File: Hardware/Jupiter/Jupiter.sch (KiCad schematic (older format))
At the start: 93 parts

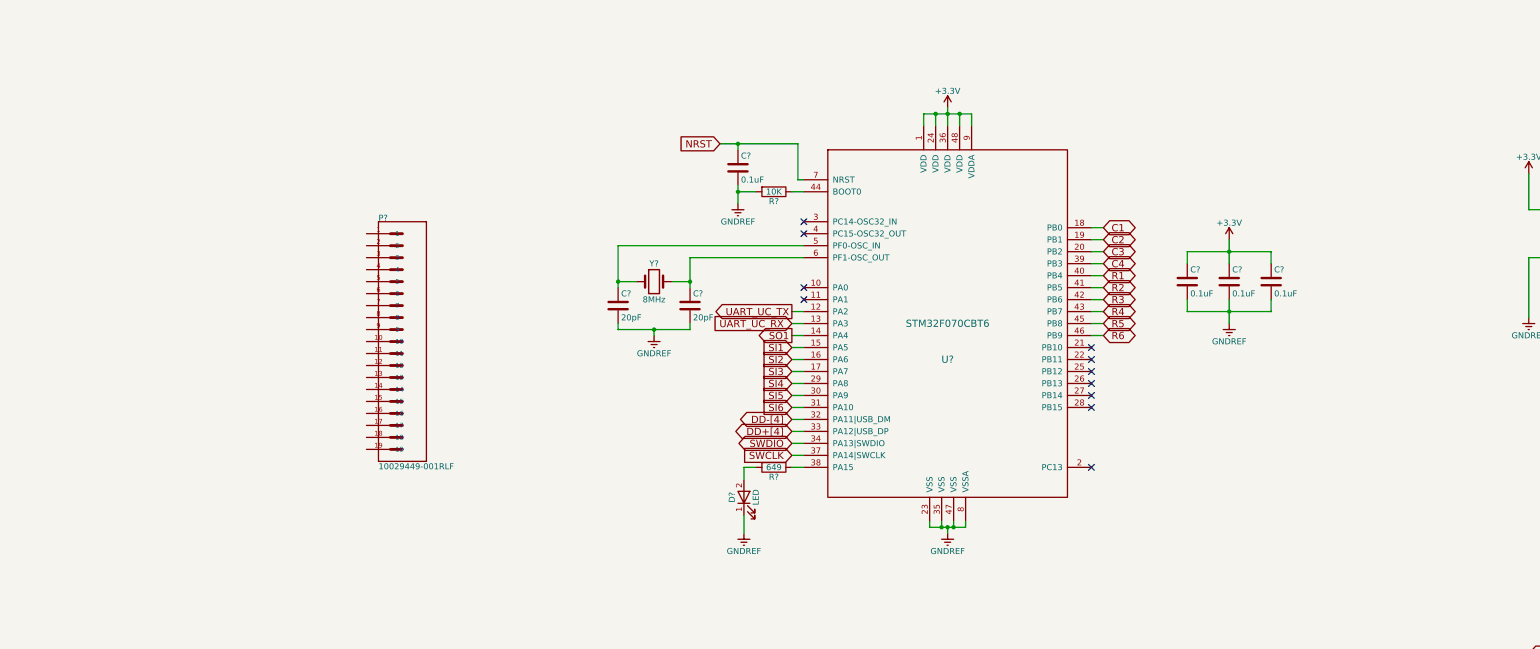
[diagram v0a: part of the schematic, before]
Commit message: Begin work for connecting HDMI transmitter interface IC to external HDMI connector.
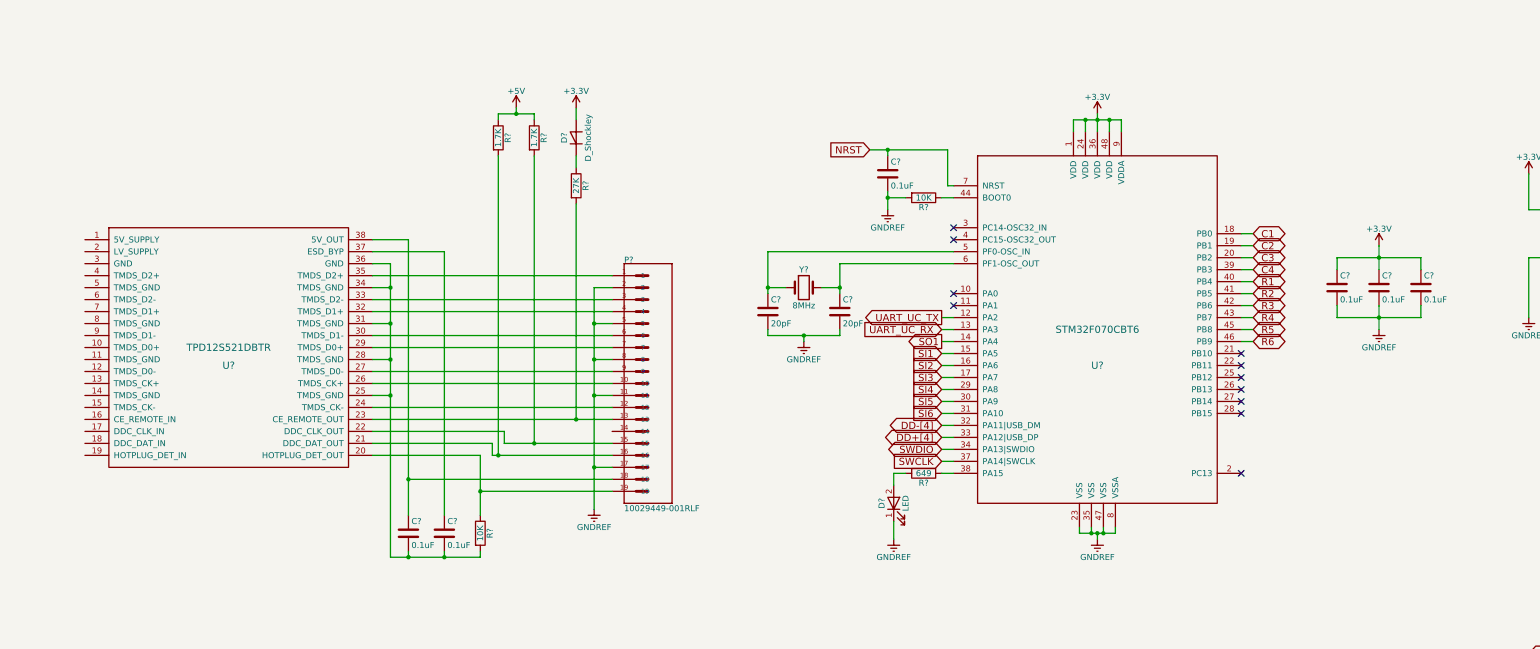
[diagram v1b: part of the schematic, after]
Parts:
- added C? (x2): 0.1uF, symbol C
- added D?: D_Shockley, symbol D_Shockley
- added R? (x2): 1.7K, symbol R
- added R?: 27K, symbol R
- added R?: 10K, symbol R
- added U?: TPD12S521DBTR, symbol TPD12S521DBTR
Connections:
- net +3V3: now also D?.2 (A)
- net +5V: now also R?.1, R?.1
- net GNDREF: now also P?.11, P?.17, P?.2, P?.5, P?.8
- net at P?.1: now also U?.35 (TMDS_D2+)
- net at P?.10: now also U?.26 (TMDS_CK+)
- net at P?.12: now also U?.24 (TMDS_CK-)
- net at P?.13: now also R?.2, U?.23 (CE_REMOTE_OUT)
- net at P?.15: now also R?.2, U?.22 (DDC_CLK_OUT)
- net at P?.16: now also R?.2, U?.21 (DDC_DAT_OUT)
- net at P?.18: now also C?.1, U?.38 (5V_OUT)
- net at P?.19: now also R?.1, U?.20 (HOTPLUG_DET_OUT)
- net at P?.3: now also U?.33 (TMDS_D2-)
- net at P?.4: now also U?.32 (TMDS_D1+)
- net at P?.6: now also U?.30 (TMDS_D1-)
- net at P?.7: now also U?.29 (TMDS_D0+)
- net at P?.9: now also U?.27 (TMDS_D0-)
- new net: C?.2, C?.2, R?.2, U?.25 (TMDS_GND), U?.28 (TMDS_GND), U?.31 (TMDS_GND), U?.34 (TMDS_GND), U?.36 (GND)
- new net: C?.1, U?.37 (ESD_BYP)
- new net: D?.1 (K), R?.1
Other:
- moved on the sheet: C?, D?, P?, R?, U?, Y?

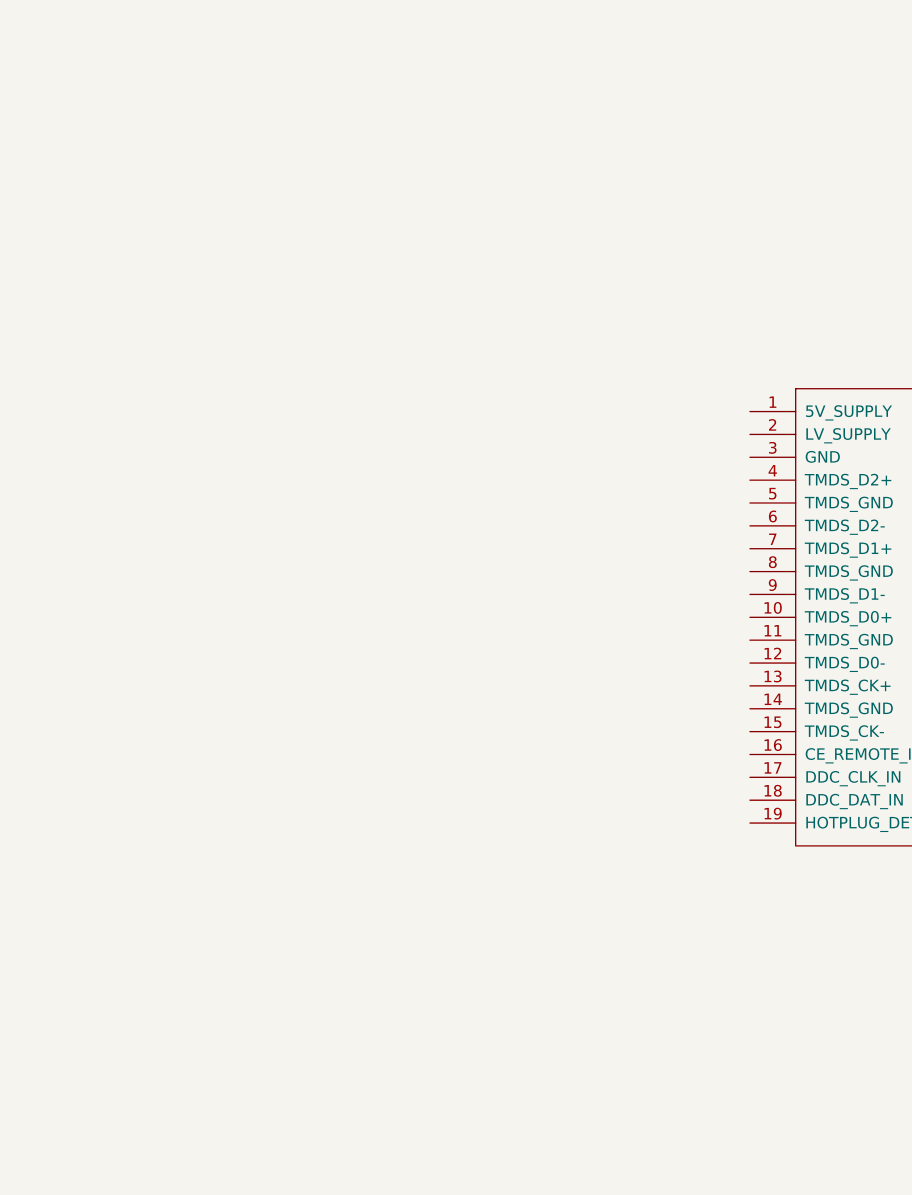
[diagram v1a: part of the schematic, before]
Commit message: Finish HDMI interfacing circuit.
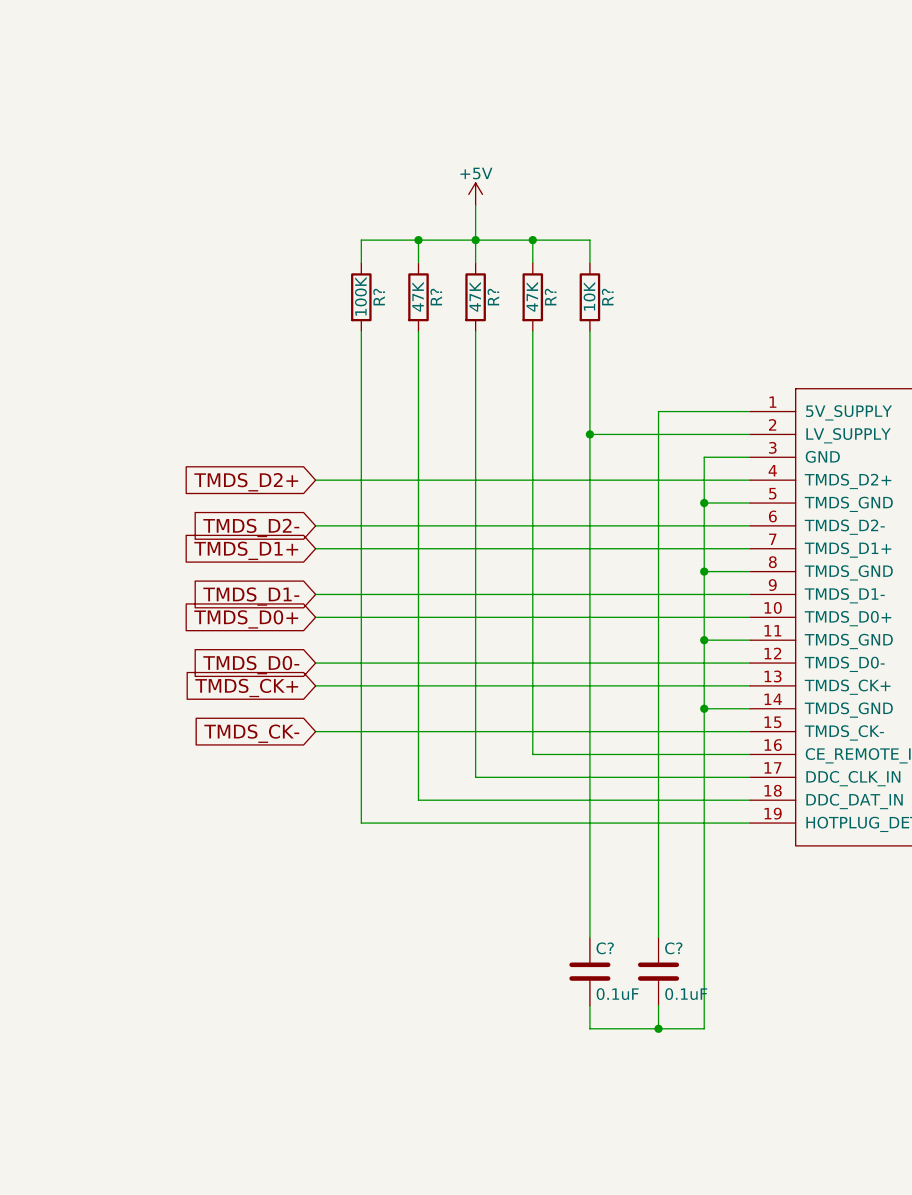
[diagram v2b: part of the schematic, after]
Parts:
- added C? (x2): 0.1uF, symbol C
- added R?: 10K, symbol R
- added R? (x3): 47K, symbol R
- added R?: 100K, symbol R
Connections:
- net +5V: now also R?.1, R?.1, R?.1, R?.1, R?.1
- net at U?.1 (5V_SUPPLY): now also C?.1
- net TMDS_D0+: now reaches U?.10 (TMDS_D0+)
- net at U?.11 (TMDS_GND): now also U?.14 (TMDS_GND), U?.3 (GND), U?.5 (TMDS_GND), U?.8 (TMDS_GND), C?.2, C?.2
- net TMDS_D0-: now reaches U?.12 (TMDS_D0-)
- net TMDS_CK+: now reaches U?.13 (TMDS_CK+)
- net TMDS_CK-: now reaches U?.15 (TMDS_CK-)
- net at U?.16 (CE_REMOTE_IN): now also R?.2
- net at U?.17 (DDC_CLK_IN): now also R?.2
- net at U?.18 (DDC_DAT_IN): now also R?.2
- net at U?.19 (HOTPLUG_DET_IN): now also R?.2
- net at U?.2 (LV_SUPPLY): now also C?.1, R?.2
- net TMDS_D2+: now reaches U?.4 (TMDS_D2+)
- net TMDS_D2-: now reaches U?.6 (TMDS_D2-)
- net TMDS_D1+: now reaches U?.7 (TMDS_D1+)
- net TMDS_D1-: now reaches U?.9 (TMDS_D1-)
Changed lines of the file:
@@
 	11550 5100 11550 7600
 Connection ~ 11550 7600
+$Comp
+L C C?
+U 1 1 5B72FE3A
+P 7700 8250
+F 0 "C?" H 7725 8350 50  0000 L CNN
+F 1 "0.1uF" H 7725 8150 50  0000 L CNN
+F 2 "" H 7738 8100 50  0001 C CNN
+F 3 "" H 7700 8250 50  0001 C CNN
+	1    7700 8250
+	1    0    0    -1
+$EndComp
+$Comp
+L C C?
+U 1 1 5B730027
+P 7400 8250
+F 0 "C?" H 7425 8350 50  0000 L CNN
+F 1 "0.1uF" H 7425 8150 50  0000 L CNN
+F 2 "" H 7438 8100 50  0001 C CNN
+F 3 "" H 7400 8250 50  0001 C CNN
+	1    7400 8250
+	1    0    0    -1
+$EndComp
+Wire Wire Line
+	7400 8400 7400 8500
+Wire Wire Line
+	7400 8500 7900 8500
+Wire Wire Line
+	7700 8500 7700 8400
+Wire Wire Line
+	7700 8100 7700 5800
+Wire Wire Line
+	7700 5800 8100 5800
+$Comp
+L R R?
+U 1 1 5B730AB0
+P 7400 5300
+F 0 "R?" V 7480 5300 50  0000 C CNN
+F 1 "10K" V 7400 5300 50  0000 C CNN
+F 2 "" V 7330 5300 50  0001 C CNN
+F 3 "" H 7400 5300 50  0001 C CNN
+	1    7400 5300
+	1    0    0    -1
+$EndComp
+Wire Wire Line
+	7400 5450 7400 8100
+Wire Wire Line
+	8100 5900 7400 5900
+Connection ~ 7400 5900
+$Comp
+L R R?
+U 1 1 5B7318F0
+P 7150 5300
+F 0 "R?" V 7230 5300 50  0000 C CNN
+F 1 "47K" V 7150 5300 50  0000 C CNN
+F 2 "" V 7080 5300 50  0001 C CNN
+F 3 "" H 7150 5300 50  0001 C CNN
+	1    7150 5300
+	1    0    0    -1
+$EndComp
+$Comp
+L R R?
+U 1 1 5B731A03
+P 6900 5300
+F 0 "R?" V 6980 5300 50  0000 C CNN
+F 1 "47K" V 6900 5300 50  0000 C CNN
+F 2 "" V 6830 5300 50  0001 C CNN
+F 3 "" H 6900 5300 50  0001 C CNN
+	1    6900 5300
+	1    0    0    -1
+$EndComp
+$Comp
+L R R?
+U 1 1 5B731AF6
+P 6650 5300
+F 0 "R?" V 6730 5300 50  0000 C CNN
+F 1 "47K" V 6650 5300 50  0000 C CNN
+F 2 "" V 6580 5300 50  0001 C CNN
+F 3 "" H 6650 5300 50  0001 C CNN
+	1    6650 5300
+	1    0    0    -1
+$EndComp
+$Comp
+L R R?
+U 1 1 5B731BE5
+P 6400 5300
+F 0 "R?" V 6480 5300 50  0000 C CNN
+F 1 "100K" V 6400 5300 50  0000 C CNN
+F 2 "" V 6330 5300 50  0001 C CNN
+F 3 "" H 6400 5300 50  0001 C CNN
+	1    6400 5300
+	1    0    0    -1
+$EndComp
+Wire Wire Line
+	7400 5150 7400 5050
+Wire Wire Line
+	7400 5050 6400 5050
+Wire Wire Line
+	6400 5050 6400 5150
+Wire Wire Line
+	6650 5150 6650 5050
+Connection ~ 6650 5050
+Wire Wire Line
+	6900 4900 6900 5150
+Connection ~ 6900 5050
+Wire Wire Line
+	7150 5150 7150 5050
+Connection ~ 7150 5050
+Wire Wire Line
+	8100 7300 7150 7300
+Wire Wire Line
+	7150 7300 7150 5450
+Wire Wire Line
+	8100 7400 6900 7400
+Wire Wire Line
+	6900 7400 6900 5450
+Wire Wire Line
+	8100 7500 6650 7500
+Wire Wire Line
+	6650 7500 6650 5450
+Wire Wire Line
+	8100 7600 6400 7600
+Wire Wire Line
+	6400 7600 6400 5450
+Wire Wire Line
+	8100 6000 7900 6000
+Wire Wire Line
+	7900 6000 7900 8500
+Connection ~ 7700 8500
+Wire Wire Line
+	8100 6200 7900 6200
+Connection ~ 7900 6200
+Wire Wire Line
+	8100 6500 7900 6500
+Connection ~ 7900 6500
+Wire Wire Line
+	8100 6800 7900 6800
+Connection ~ 7900 6800
+Wire Wire Line
+	8100 7100 7900 7100
+Connection ~ 7900 7100
+$Comp
+L +5V #PWR?
+U 1 1 5B734AEA
+P 6900 4900
+F 0 "#PWR?" H 6900 4750 50  0001 C CNN
+F 1 "+5V" H 6900 5040 50  0000 C CNN
+F 2 "" H 6900 4900 50  0001 C CNN
+F 3 "" H 6900 4900 50  0001 C CNN
+	1    6900 4900
+	1    0    0    -1
+$EndComp
+Text GLabel 6200 6100 0    60   Input ~ 0
+TMDS_D2+
+Wire Wire Line
+	6200 6100 8100 6100
+Text GLabel 6200 6300 0    60   Input ~ 0
+TMDS_D2-
+Wire Wire Line
+	6200 6300 8100 6300
+Text GLabel 6200 6400 0    60   Input ~ 0
+TMDS_D1+
+Wire Wire Line
+	6200 6400 8100 6400
+Text GLabel 6200 6600 0    60   Input ~ 0
+TMDS_D1-
+Wire Wire Line
+	6200 6600 8100 6600
+Text GLabel 6200 6700 0    60   Input ~ 0
+TMDS_D0+
+Wire Wire Line
+	6200 6700 8100 6700
+Text GLabel 6200 6900 0    60   Input ~ 0
+TMDS_D0-
+Text GLabel 6200 7000 0    60   Input ~ 0
+TMDS_CK+
+Text GLabel 6200 7200 0    60   Input ~ 0
+TMDS_CK-
+Wire Wire Line
+	6200 7200 8100 7200
+Wire Wire Line
+	8100 7000 6200 7000
+Wire Wire Line
+	6200 6900 8100 6900
 $EndSCHEMATC

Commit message: Finish HDMI interface.
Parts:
- added Q?: Q_NMOS_GSD, symbol Q_NMOS_GSD
- added R?: 100K, symbol R
- added R?: 4.7K, symbol R
- added SW?: SW_DPST_x2, symbol SW_DPST_x2
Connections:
- net +1V8: now also R?.1
- net +3V3: now also R?.1, R?.1, R?.1, R?.1, R?.1
- net +5V: now also SW?.2 (B); no longer J?.1, R?.1, R?.1, R?.1, R?.1, R?.1
- net GNDREF: now also Q?.2 (S)
- net CEC: now reaches R?.2, U?.16 (CE_REMOTE_IN)
- net DDC_CLK: now reaches R?.2, U?.17 (DDC_CLK_IN)
- net DDC_DAT: now reaches R?.2, U?.18 (DDC_DAT_IN)
- net at R?.2, U?.19 (HOTPLUG_DET_IN): now also R?.1
- new net: J?.1, SW?.1 (A)
- new net: Q?.1 (G), R?.2
- new net HOTPLUG_DET_1V8: Q?.3 (D), R?.2
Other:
- moved on the sheet: C?, D?, J?, L?, P?, R?, U?, Y?

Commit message: Add pinouts to right-hand side of SO-DIMM connector.
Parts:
- added C?: 4.7uF, symbol C
- added R?: 0, symbol R
- added R? (x4): 100K, symbol R
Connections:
- net +1V8: now also MD?.184 (1V8), MD?.186 (1V8)
- net +3V3: now also MD?.190 (VDAC), MD?.192 (3V3), MD?.194 (3V3), MD?.198 (VBAT), MD?.200 (VBAT), MD?.40 (GPIO0-27_VDD), MD?.42 (GPIO28-45_VDD), R?.1
- net GNDREF: now also MD?.104 (GND), MD?.110 (GND), MD?.116 (GND), MD?.122 (GND), MD?.134 (GND), MD?.14 (GND), MD?.140 (GND), MD?.146 (GND), MD?.152 (GND), MD?.164 (GND), MD?.168 (USB_OTGID), MD?.170 (GND), MD?.188 (GND), MD?.196 (GND), MD?.20 (GND), MD?.26 (GND), MD?.32 (GND), MD?.38 (GND), MD?.44 (GND), MD?.50 (GND), MD?.56 (GND), MD?.62 (GND), MD?.68 (GND), MD?.74 (GND), MD?.8 (GND), MD?.80 (GND), MD?.86 (GND), MD?.92 (GND), MD?.98 (GND), C?.2, R?.1, R?.1, R?.1, R?.1
- net HOTPLUG_DET_1V8: now also MD?.88 (HDMI_HPD_N_1V8)
- net SDX_CLK: now reaches MD?.10 (SDX_CLK)
- net SDX_CMD: now reaches MD?.12 (NC)
- net SDX_D0: now reaches MD?.16 (NC)
- net SDX_D1: now reaches MD?.18 (NC)
- net SDX_D2: now reaches MD?.22 (NC)
- net SDX_D3: now reaches MD?.24 (NC)
- net at MD?.28 (GPIO28): now also R?.2
- net at MD?.30 (GPIO29): now also R?.2
- net at MD?.4 (SDX_VDD): now also MD?.6 (SDX_VDD), C?.1, R?.2
- net at MD?.82 (GPIO44): now also R?.2
- net at MD?.84 (GPIO45): now also R?.2
- no-connect marks 19 -> 67
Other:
- moved on the sheet: C?, D?, MD?, P?, Q?, R?, U?, Y?

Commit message: Fill in more details on Compute Module connector.
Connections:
- net +3V3: now also MD?.39 (GPIO0-27_VDD), MD?.41 (GPIO28-45_VDD)
- net CS: now also MD?.27 (GPIO8)
- net GNDREF: now also MD?.1 (GND), MD?.13 (GND), MD?.19 (GND), MD?.25 (GND), MD?.31 (GND), MD?.37 (GND), MD?.43 (GND), MD?.49 (GND), MD?.7 (GND)
- net MISO: now also MD?.29 (GPIO9)
- net MOSI: now also MD?.33 (GPIO10)
- net SCLK: now also MD?.35 (GPIO11)
- no-connect marks 67 -> 77
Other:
- moved on the sheet: C?, D?, J?, L?, P?, Q?, R?, RN?, U?, Y?

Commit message: Finish Compute Module wiring.
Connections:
- net +1V8: now also MD?.183 (1V8), MD?.185 (1V8)
- net +3V3: now also MD?.189 (VDAC), MD?.191 (3V3), MD?.193 (3V3), MD?.197 (VBAT), MD?.199 (VBAT)
- net CEC: now also MD?.171 (HDMI_CEC)
- net D+: now also MD?.165 (USB_DP)
- net D-: now also MD?.167 (USB_DM)
- net DDC_CLK: now also MD?.175 (HDMI_SCL)
- net DDC_DAT: now also MD?.173 (HDMI_SDA)
- net GNDREF: now also MD?.103 (GND), MD?.109 (GND), MD?.115 (GND), MD?.121 (GND), MD?.127 (GND), MD?.133 (GND), MD?.139 (GND), MD?.145 (GND), MD?.151 (GND), MD?.157 (GND), MD?.163 (GND), MD?.169 (GND), MD?.181 (GND), MD?.182 (GND), MD?.187 (GND), MD?.195 (GND), MD?.55 (GND), MD?.61 (GND), MD?.67 (GND), MD?.73 (GND), MD?.79 (GND), MD?.85 (GND), MD?.91 (GND), MD?.97 (GND)
- net INT: now also MD?.83 (GPIO25)
- net TMDS_CK+: now also MD?.113 (HDMI_CLK_P)
- net TMDS_CK-: now also MD?.111 (HDMI_CLK_N)
- net TMDS_D0+: now also MD?.119 (HDMI_D0_P)
- net TMDS_D0-: now also MD?.117 (HDMI_D0_N)
- net TMDS_D1+: now also MD?.125 (HDMI_D1_P)
- net TMDS_D1-: now also MD?.123 (HDMI_D1_N)
- net TMDS_D2+: now also MD?.131 (HDMI_D2_P)
- net TMDS_D2-: now also MD?.129 (HDMI_D2_N)
- no-connect marks 77 -> 108
